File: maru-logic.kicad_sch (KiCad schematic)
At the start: 18 parts, among them J1 USB-C, U1 4011, U2 4011, U3 4011, U5 4011

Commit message: routing done
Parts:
- added C12, C3, C6, C9: 100n, Capacitor_SMD:C_0402_1005Metric, symbol Device:C
- renumbered C8 to C10, C9 to C11, C3 to C2, C6 to C7, C7 to C8, R2 to R1, R3 to R2, R1 to R3, R9 to R4, R10 to R5, U3 to U2, U2 to U3, U5 to U4
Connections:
- net VDD: now also C12.1, C3.1, C6.1, C9.1
- net VSS: now also C12.2, C3.2, C6.2, C9.2
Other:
- moved on the sheet: R3, R4, R5

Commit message: ready to order
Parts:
- added C12, C16, C4, C8: 100n, Capacitor_SMD:C_0402_1005Metric, symbol Device:C
- added H1, H2, H5, H6: JLC, mark:JLCPCB_ToolingHole_1152_1300_1400_1650, symbol Mechanical:MountingHole
- added H3, H4, H7, H8: MountingHole, MountingHole:MountingHole_2.2mm_M2_ISO7380, symbol Mechanical:MountingHole
- U1, U2, U3, U4: value 4011 -> 4093; symbol 4xxx:4011 -> 4xxx:HEF4093B; JLC C194334 -> C194332
- renumbered C8 to C10, C9 to C11, C10 to C13, C11 to C14, C12 to C15, C4 to C5, C5 to C6, C6 to C7, C7 to C9, R3 to R1, R4 to R2, R5 to R3, R1 to R4, R2 to R5
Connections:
- net VDD: now also C12.1, C16.1, C4.1, C8.1
- net VSS: now also C12.2, C16.2, C4.2, C8.2
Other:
- note removed: "TODO: Add a T- or RS- flipflop with lights on each internal connection too"
- moved on the sheet: C1, C10, C11, C13, C14, C15, C2, C3, C5, C6, C7, C9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

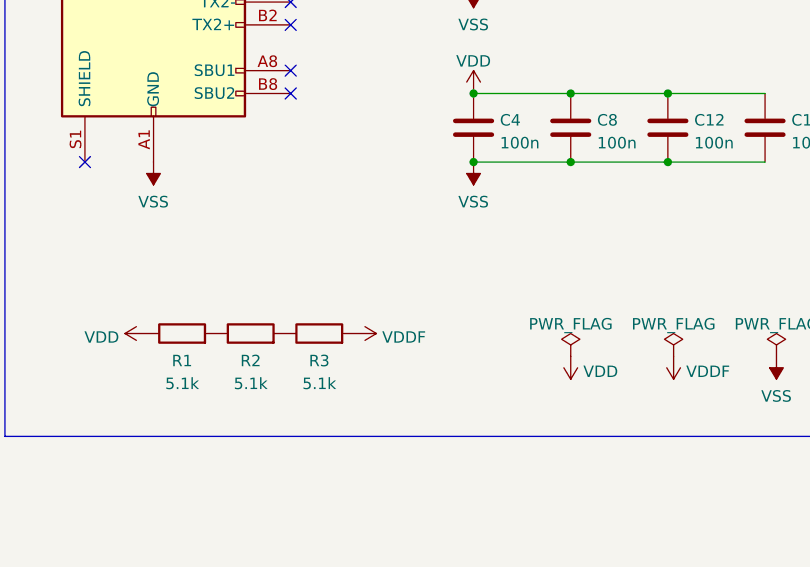
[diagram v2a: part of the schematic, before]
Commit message: started fixing issues from V1
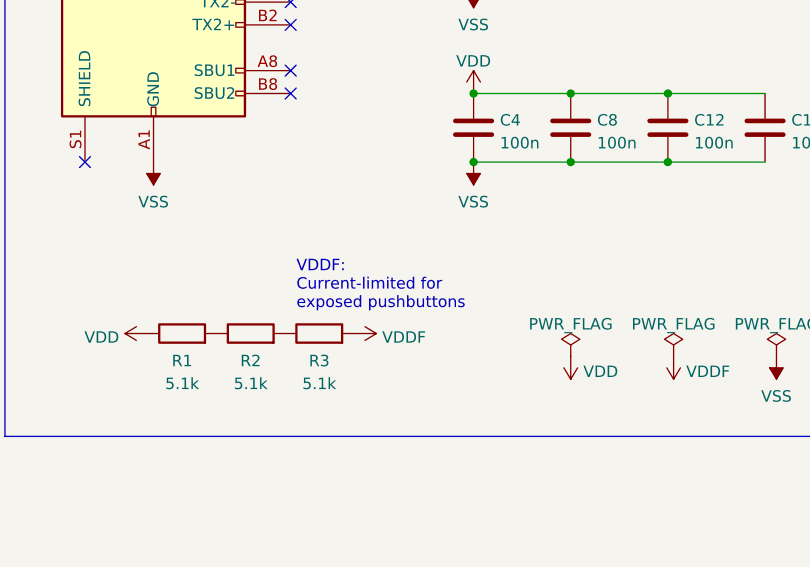
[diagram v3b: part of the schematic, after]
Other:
- note added: "VDDF: Current-limited for exposed pushbuttons"

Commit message: pre-re-layout
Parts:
- removed C1, C10, C13, C2, C5, C6, C9: 100n, Capacitor_SMD:C_0402_1005Metric, symbol Device:C
- removed R1, R2, R3: 5.1k, Resistor_SMD:R_0402_1005Metric, symbol Device:R
- H101: renamed from H1; JLC (none) -> -
- H102: renamed from H2; JLC (none) -> -
- H103: renamed from H3; JLC (none) -> -
- H104: renamed from H4; JLC (none) -> -
- H105: renamed from H5; JLC (none) -> -
- H106: renamed from H6; JLC (none) -> -
- H107: renamed from H7; JLC (none) -> -
- H108: renamed from H8; JLC (none) -> -
- renumbered C14 to C101, C3 to C102, C4 to C103, C7 to C104, C8 to C105, C11 to C106, C12 to C107, C15 to C108, C16 to C109, J1 to J101, R4 to R101, R5 to R102, U1 to U101, U2 to U102, U3 to U103, U4 to U104
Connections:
- net AND_X: no longer U103.9
- net NOT_X: no longer U103.8
- net OR_X: no longer U103.12
- net XOR_X: no longer U103.13
- new net AND_Y: U103.9
- new net NOT_Y: U103.8
- new net OR_Y: U103.12
- new net XOR_Y: U103.13
- no-connect marks 15 -> 17
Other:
- sheet Toggle Button 1 renamed Button NOT_A
- sheet Toggle Button 2 renamed Button AND_A
- sheet Toggle Button 3 renamed Button AND_B
- sheet Toggle Button 4 renamed Button OR_A
- sheet Toggle Button 5 renamed Button OR_B
- sheet Toggle Button 6 renamed Button XOR_A
- sheet Toggle Button 7 renamed Button XOR_B
- removed sheet Output LEDs
- added sheet Chain ALL_X (led_chain_5.kicad_sch)
- added sheet Chain ALL_Y1 (led_chain_6.kicad_sch)
- added sheet Chain ALL_Y2 (led_chain_6.kicad_sch)
- added sheet Chain AND_A (led_chain_5.kicad_sch)
- added sheet Chain AND_B (led_chain_5.kicad_sch)
- added sheet Chain AND_X (led_chain_6.kicad_sch)
- added sheet Chain NOT_A (led_chain_5.kicad_sch)
- added sheet Chain NOT_X (led_chain_6.kicad_sch)
- added sheet Chain OR_A (led_chain_5.kicad_sch)
- added sheet Chain OR_B (led_chain_5.kicad_sch)
- added sheet Chain OR_X (led_chain_5.kicad_sch)
- added sheet Chain XOR_A (led_chain_5.kicad_sch)
- added sheet Chain XOR_B (led_chain_5.kicad_sch)
- added sheet Chain XOR_X (led_chain_5.kicad_sch)
- note added: "A = input B = input X = output (immediate) Y = output (delayed)"
- note added: "Inputs"
- note added: "Outputs"
- note removed: "LED state indicators (gate outputs) Inputs are included in the buttons"
- note removed: "Toggle buttons"
- note removed: "VDDF: Current-limited for exposed pushbuttons"
- moved on the sheet: C101, C102, C103, C104, C105, C106, C107, C108, C109, H101, H102, H103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

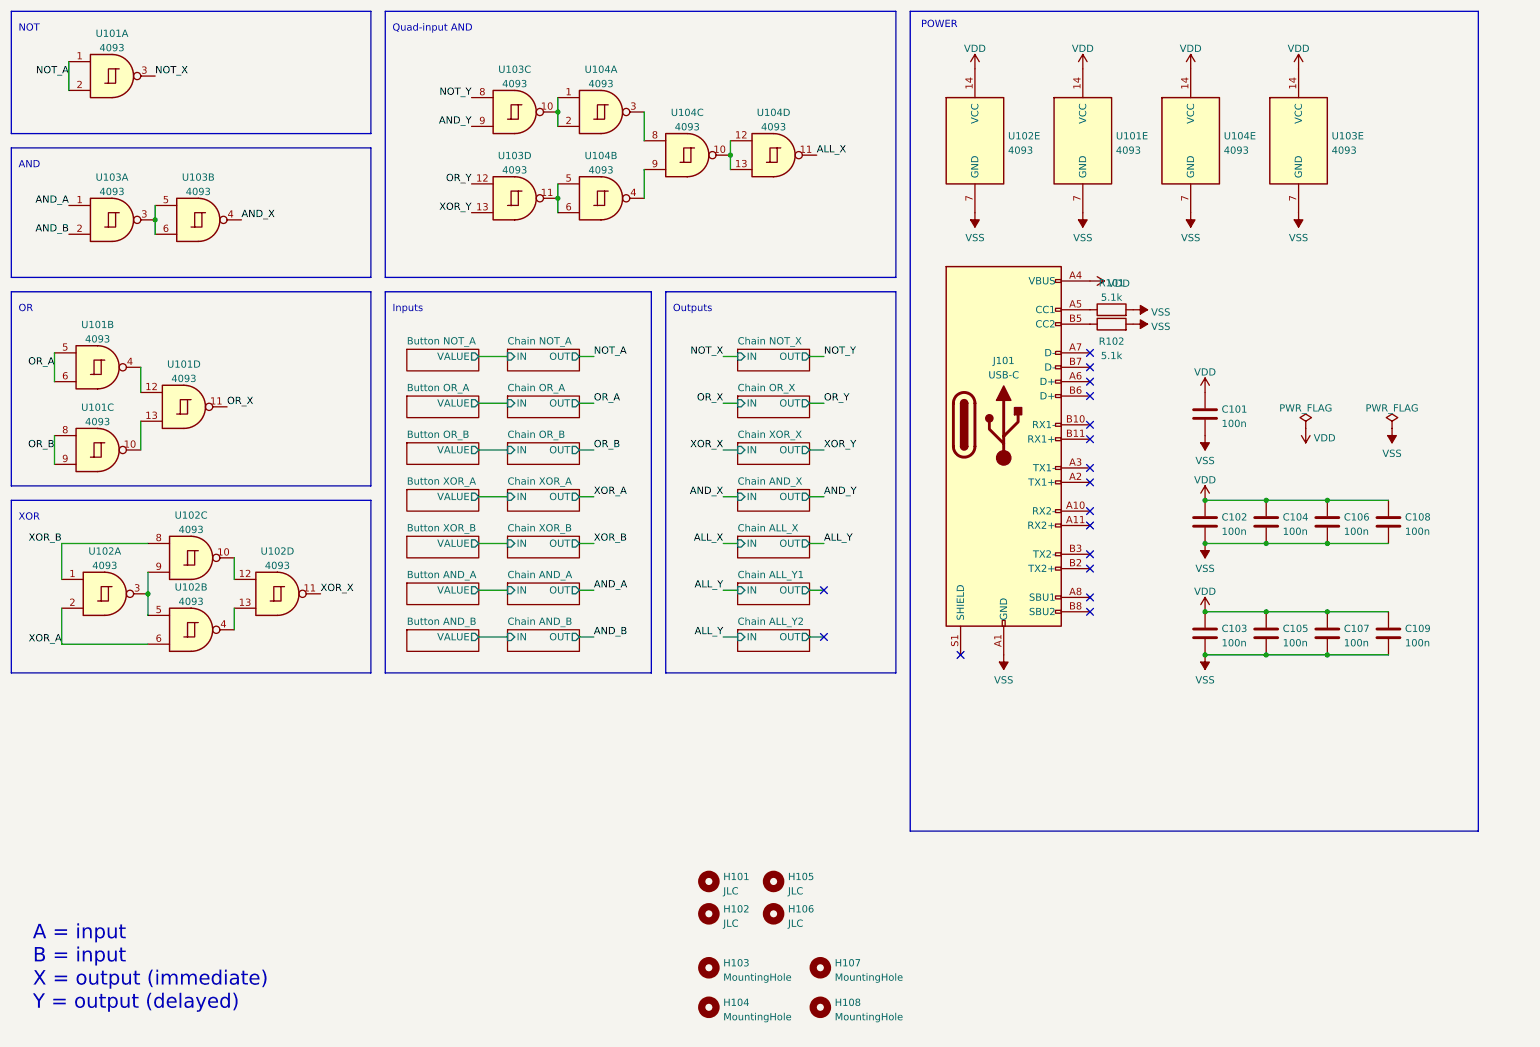
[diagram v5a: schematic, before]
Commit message: pcb-text plugin applied, next step is to write a replicate layout plugin that actually works
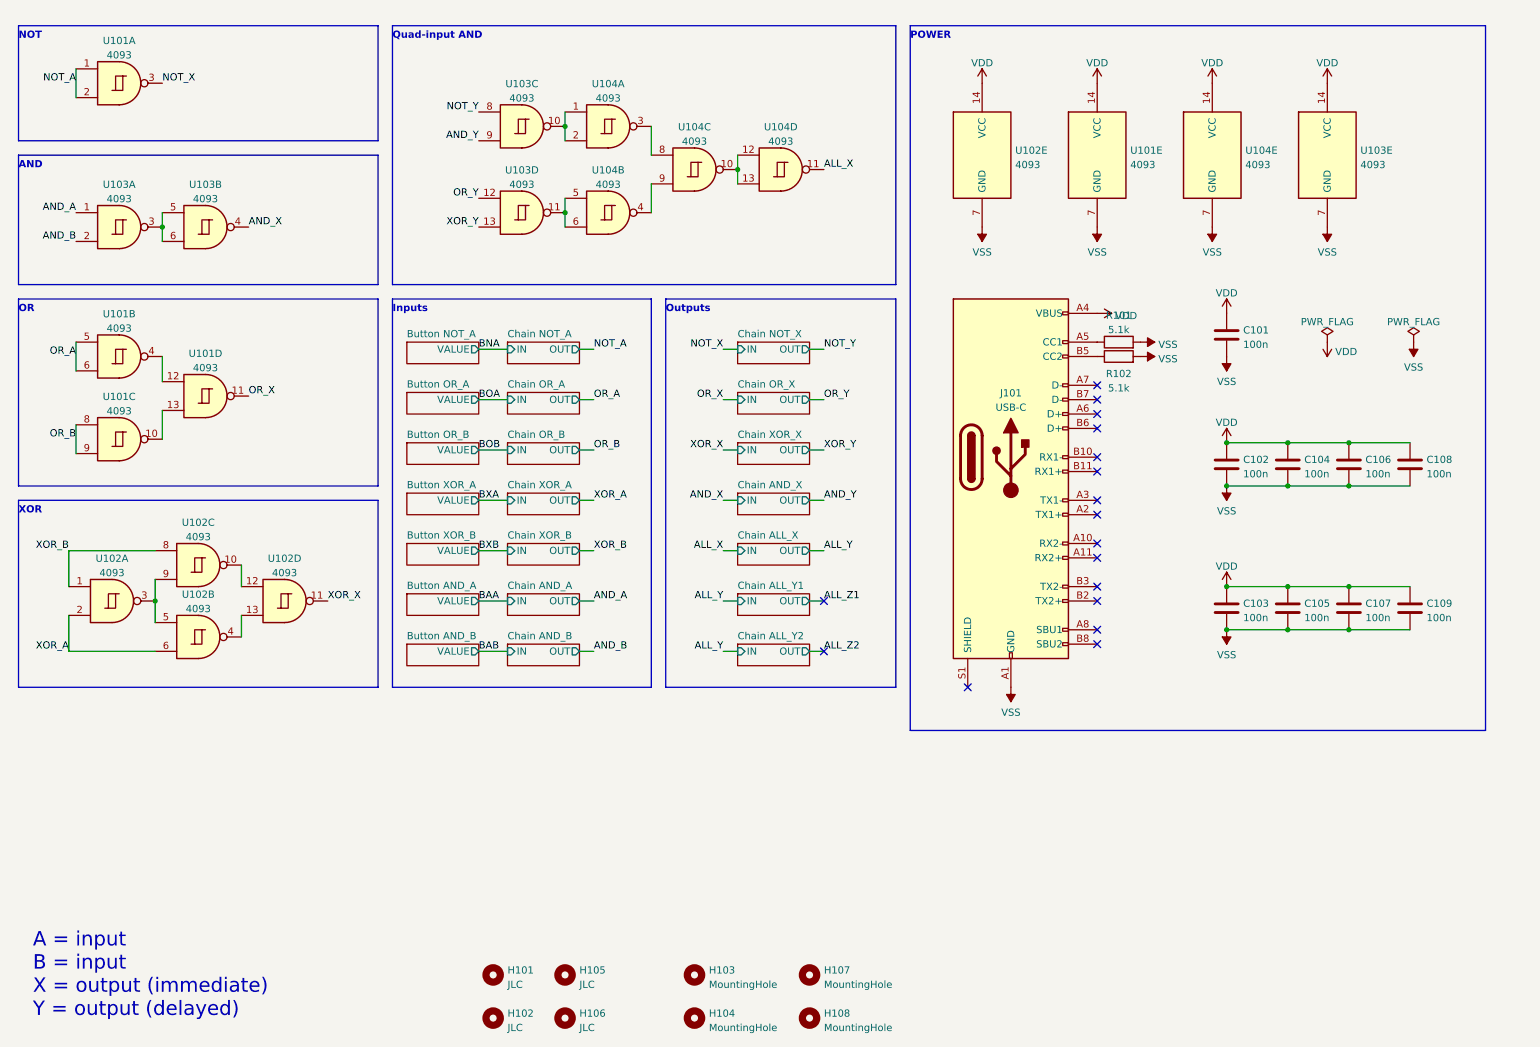
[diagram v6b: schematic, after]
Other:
- moved on the sheet: C101, C102, C103, C104, C105, C106, C107, C108, C109, H101, H102, H103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

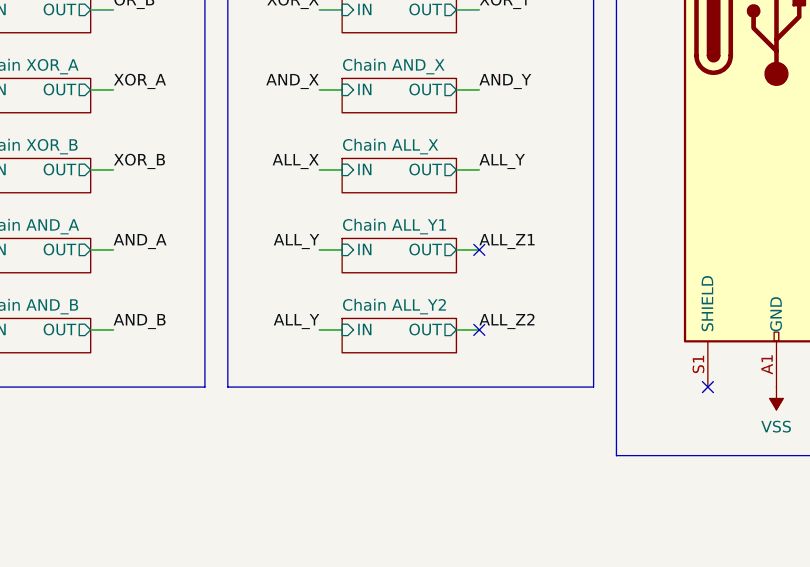
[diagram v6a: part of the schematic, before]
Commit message: layout done, starting case
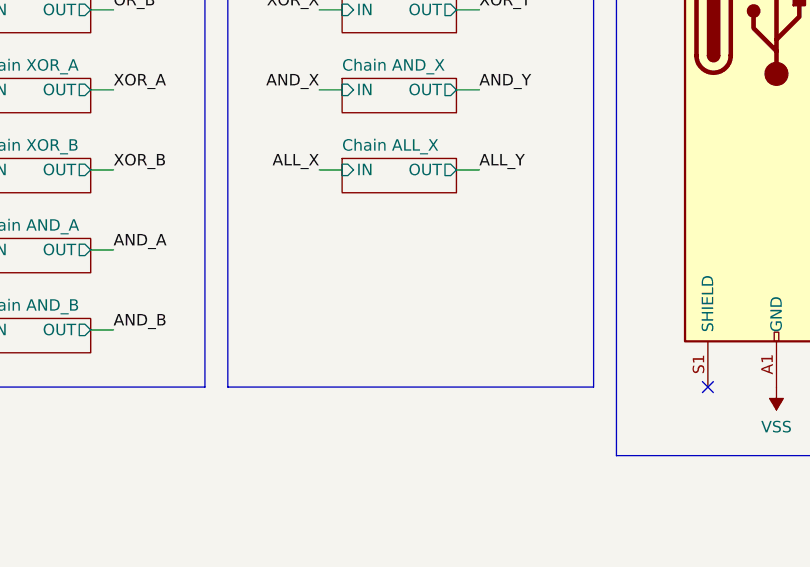
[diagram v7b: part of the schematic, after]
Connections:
- no-connect marks 17 -> 15
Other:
- removed sheet Chain ALL_Y1
- removed sheet Chain ALL_Y2
